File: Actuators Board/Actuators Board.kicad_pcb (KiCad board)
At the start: 2 copper layers, 50 x 50 mm, 101 parts, among them IC1 BD62120AEFJ-E2, J10 Conn_01x02_Male, J3 USB_C_Receptacle_USB2.0, J4 Conn_01x03_Male, J5 Conn_01x06_Male, J9 Conn_01x02_Male, Q1 MMDT2222A, Q2 SI2366DS, U1 ESP32-PICO-D4, U2 TPS54233D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

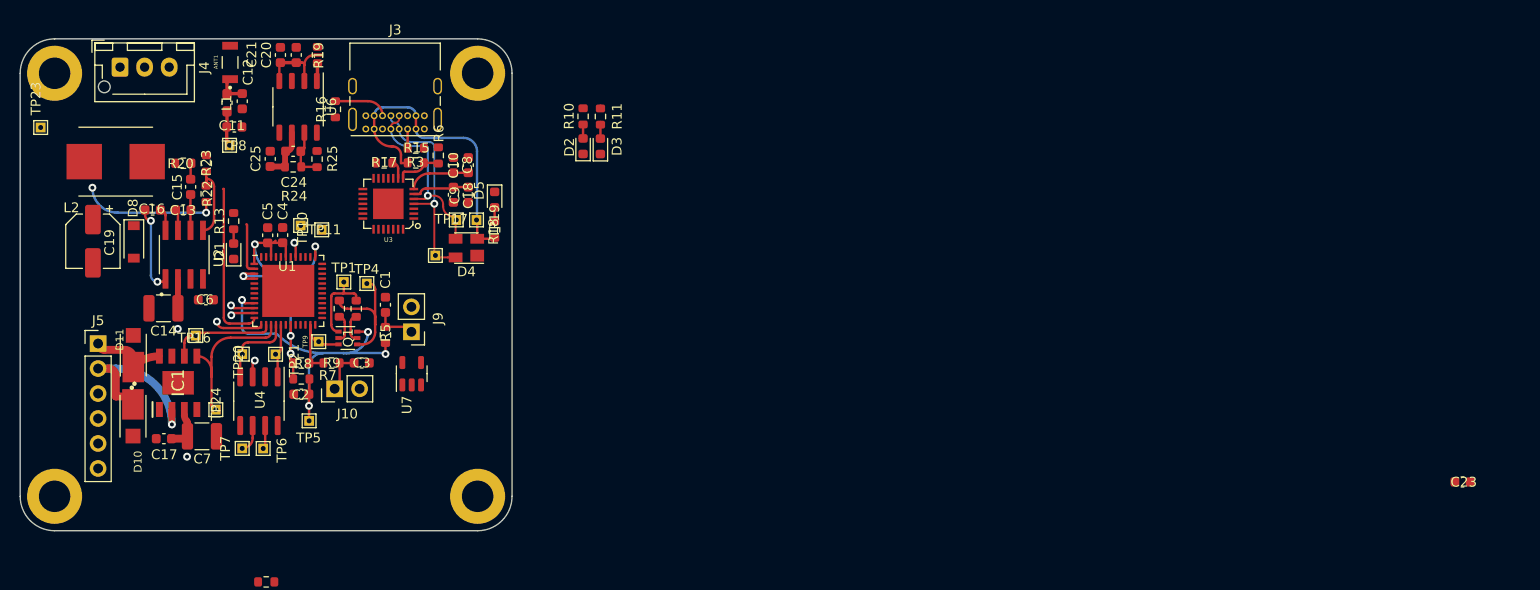
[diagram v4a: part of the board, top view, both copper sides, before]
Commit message: Added (unfilled) ground zones + antenna keepout
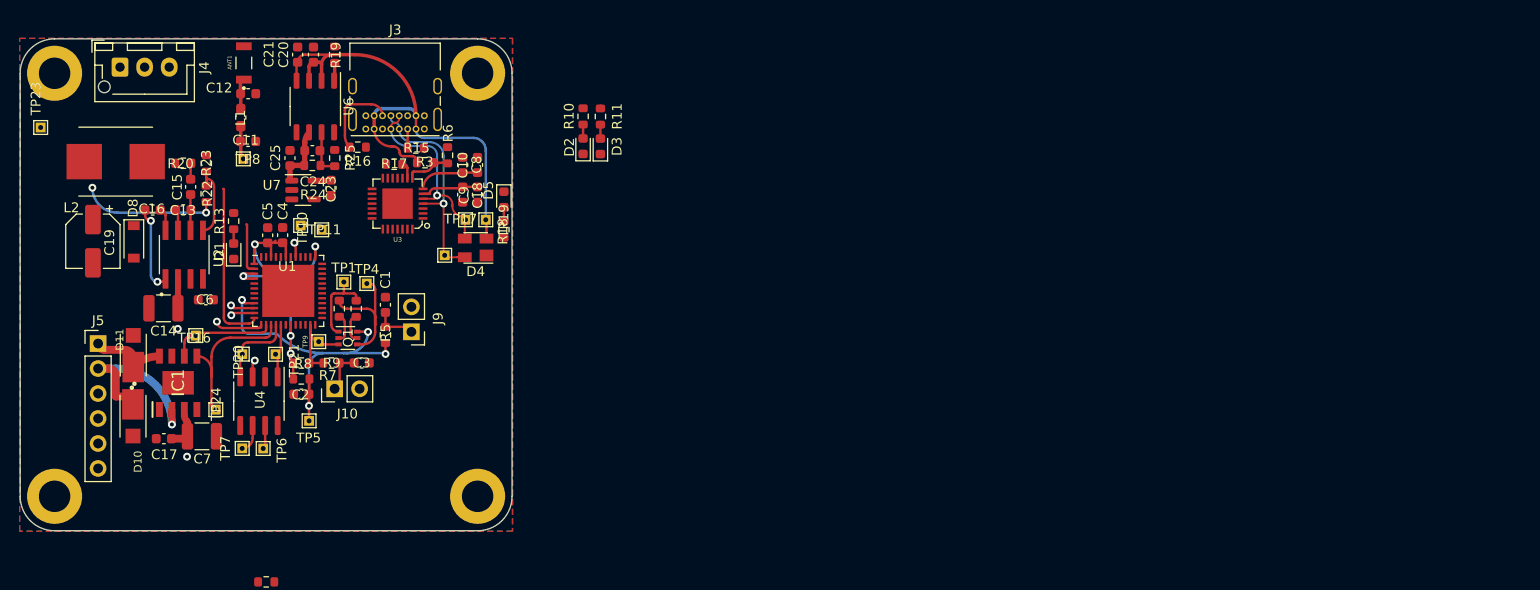
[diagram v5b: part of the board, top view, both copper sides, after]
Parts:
- moved C23 118.8 mm to (86.6, 45.1), turned to -90 degrees
- moved U7 21.7 mm to (83.8, 45.4), turned to 0 degrees
- moved R16 4.47 mm to (89.3, 41.0), turned to 180 degrees
- moved L1 2.05 mm to (77.4, 38.0)
- moved C11 2.03 mm to (78.2, 40.4)
- moved C25 2.01 mm to (82.4, 42.1)
- moved TP8 1.97 mm to (77.7, 42.2)
- moved R24 1.96 mm to (84.7, 42.9)
- moved C24 1.95 mm to (84.7, 41.4)
- moved R25 1.80 mm to (87.0, 42.1)
- moved C20 1.75 mm to (84.8, 31.6)
- moved C21 1.75 mm to (83.2, 31.6)
- moved R19 1.75 mm to (87.0, 31.6)
- moved U6 1.75 mm to (85.0, 36.9)
- moved ANT1 1.40 mm to (77.7, 32.4)
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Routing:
- net VBUS: track 40.1 -> 55.4 mm
- net Net-(J3-PadB5): track 5.58 -> 8.62 mm
- net +3V3: track 52.5 -> 54.2 mm
- net Net-(C24-Pad2): track 5.39 -> 6.52 mm
- net /USB -> UART/Data-: track 19.0 -> 19.5 mm
- added copper zone on B.Cu, net GND
- added copper zone on F.Cu, net GND

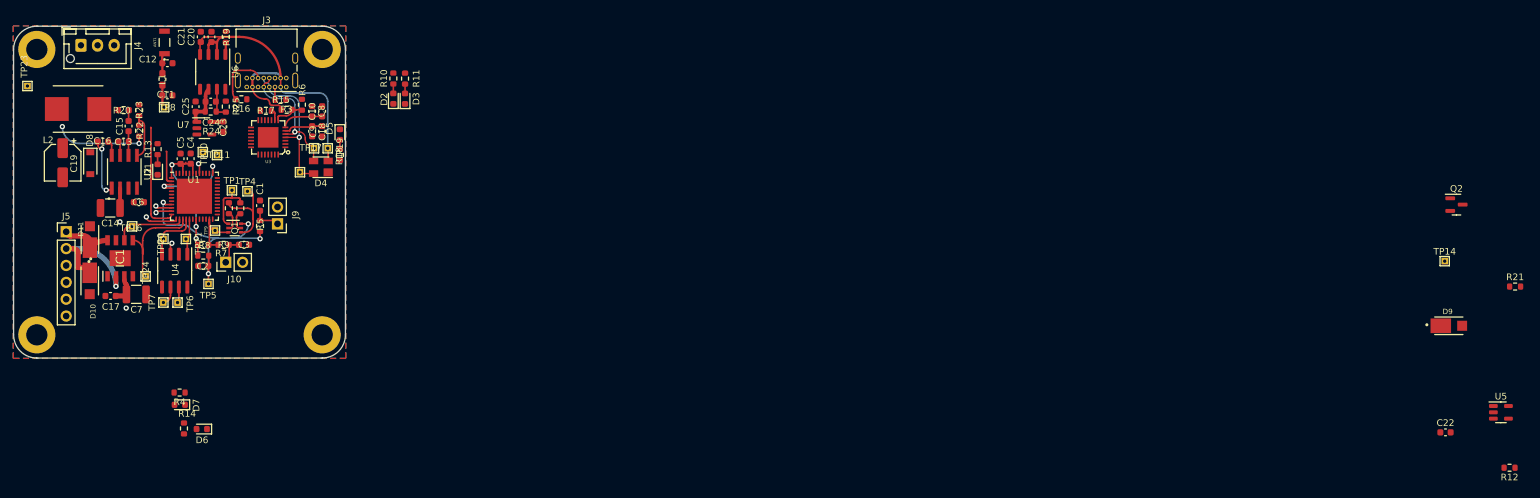
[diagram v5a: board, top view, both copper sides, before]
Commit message: Completed board layout
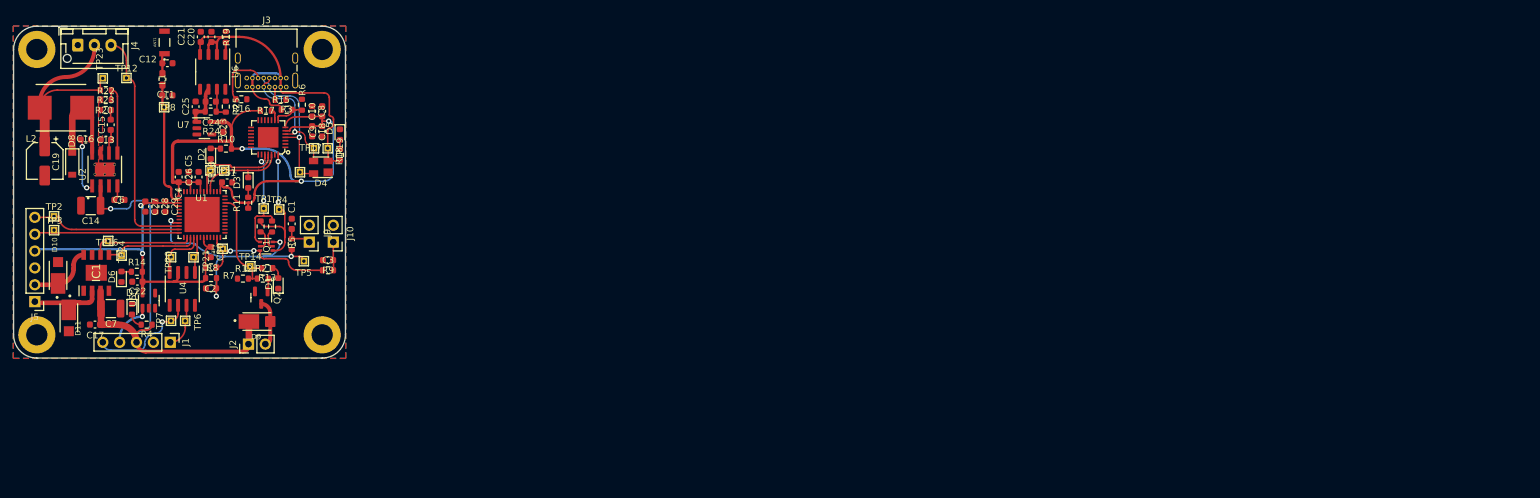
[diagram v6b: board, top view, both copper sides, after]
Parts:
- added ?: , , F.Cu at (93.7, 74.5)
- added C26: 100pF, Capacitor_SMD:C_0603_1608Metric, F.Cu at (82.9, 52.7)
- added C27: 10uF, Capacitor_SMD:C_0603_1608Metric, F.Cu at (74.8, 57.2)
- added C28: 1uF, Capacitor_SMD:C_0603_1608Metric, F.Cu at (76.4, 57.2)
- added C29: 0.1uF, Capacitor_SMD:C_0603_1608Metric, F.Cu at (77.9, 57.2)
- added C30: 0.1uF, Capacitor_SMD:C_0603_1608Metric, F.Cu at (84.7, 64.0)
- added C31: 0.1uF, Capacitor_SMD:C_0603_1608Metric, F.Cu at (87.2, 53.5)
- added J1: Conn_01x05_Male, Connector_PinHeader_2.54mm:PinHeader_1x05_P2.54mm_Vertical, F.Cu at (78.6, 77.6)
- added J2: Solenoid(Sol), Connector_PinHeader_2.54mm:PinHeader_1x02_P2.54mm_Vertical, F.Cu at (90.4, 77.9)
- added TP12: TestPoint, TestPoint:TestPoint_THTPad_1.0x1.0mm_Drill0.5mm, F.Cu at (72.0, 37.8)
- added TP2: TestPoint, TestPoint:TestPoint_THTPad_1.0x1.0mm_Drill0.5mm, F.Cu at (61.1, 58.6)
- added TP3: TestPoint, TestPoint:TestPoint_THTPad_1.0x1.0mm_Drill0.5mm, F.Cu at (61.1, 60.7)
- C4: value 10uF -> 0.1uF
- C5: value 0.1uF -> 1uF
- U2: footprint iclr:SOIC127P599X175-8N -> iclr:SOIC127P600X170-9N
- moved U5 204.4 mm to (75.4, 71.3), turned to 90 degrees
- moved C22 198.4 mm to (73.7, 68.5), turned to 180 degrees
- moved R12 193.0 mm to (89.6, 68.0)
- moved R21 188.7 mm to (92.6, 68.0), turned to 180 degrees
- moved Q2 180.6 mm to (92.3, 70.9), turned to -90 degrees
- moved TP14 180.0 mm to (90.7, 66.2)
- moved D9 179.6 mm to (91.7, 74.5)
- moved R11 30.1 mm to (90.3, 56.6), turned to 90 degrees
- moved D2 28.7 mm to (84.7, 49.2)
- moved R10 27.3 mm to (87.0, 48.5), turned to 180 degrees
- moved D3 26.8 mm to (90.3, 53.6), turned to -90 degrees
- moved D6 25.9 mm to (71.2, 67.8), turned to 90 degrees
- moved D1 25.0 mm to (94.9, 68.8)
- moved R14 24.7 mm to (73.6, 67.0), turned to 0 degrees
- moved R13 24.4 mm to (93.2, 66.5), turned to 180 degrees
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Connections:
- C4 pad 1: GND -> +3V3
- C4 pad 2: +3V3 -> GND
- IC1 pad 2: /Motor- -> /Motor+
- IC1 pad 8: /Motor+ -> /Motor-
- U1 pad 10: /Hall1 -> /ServoPWM
- U1 pad 12: /SolEN -> /Hall1
- U1 pad 13: /ServoPWM -> unconnected-(U1-Pad13)
- U1 pad 34: unconnected-(U1-Pad34) -> /SolEN
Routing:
- net +3V3: track 54.2 -> 153.6 mm, vias 6 -> 5
- net +24V: track 8.02 -> 73.4 mm, vias 2 -> 1
- net /ServoPWM: track 5.02 -> 35.4 mm, vias 1 -> 0
- net /Hall2: track 2.46 -> 22.9 mm, vias 1 -> 0
- net /Hall1: track 2.51 -> 22.4 mm, vias 1 -> 0
- net +6V: track 14.2 -> 32.5 mm, vias 2 -> 0
- net /RXD: track 1.56 -> 15.8 mm, vias 1 -> 0
- net /TXD: track 0.00 -> 14.0 mm
- net /CAN_LOW: track 2.89 -> 16.5 mm, vias 0 -> 1
- net /BOOT: track 9.52 -> 22.7 mm, vias 0 -> 2
- net Net-(C16-Pad2): track 2.34 -> 15.0 mm
- net /LNA_IN: track 8.61 -> 19.0 mm
- net /Motor-: track 19.5 -> 10.6 mm, vias 1 -> 0
- net /DTR: track 13.3 -> 22.2 mm, vias 0 -> 2
- net /RTS: track 8.47 -> 17.0 mm, vias 0 -> 2
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
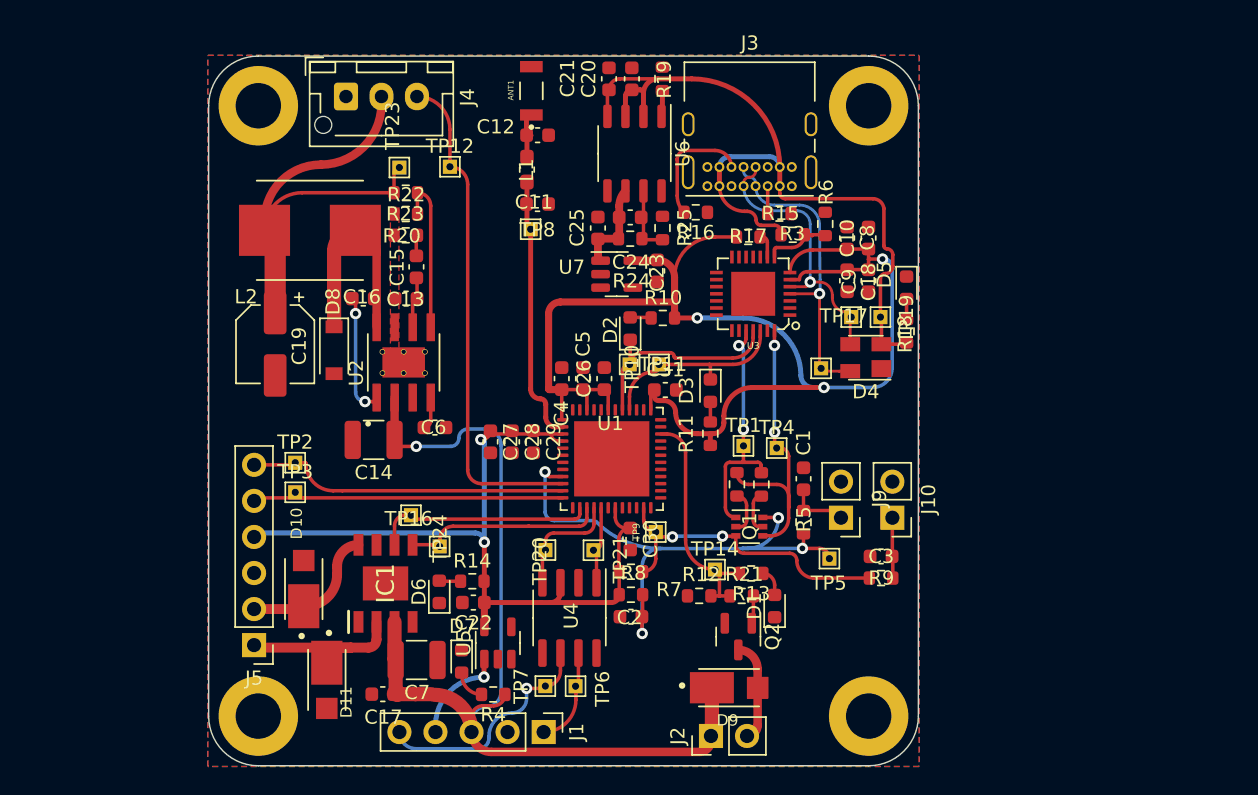
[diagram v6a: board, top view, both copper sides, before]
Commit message: Moved esp closer to the antenna
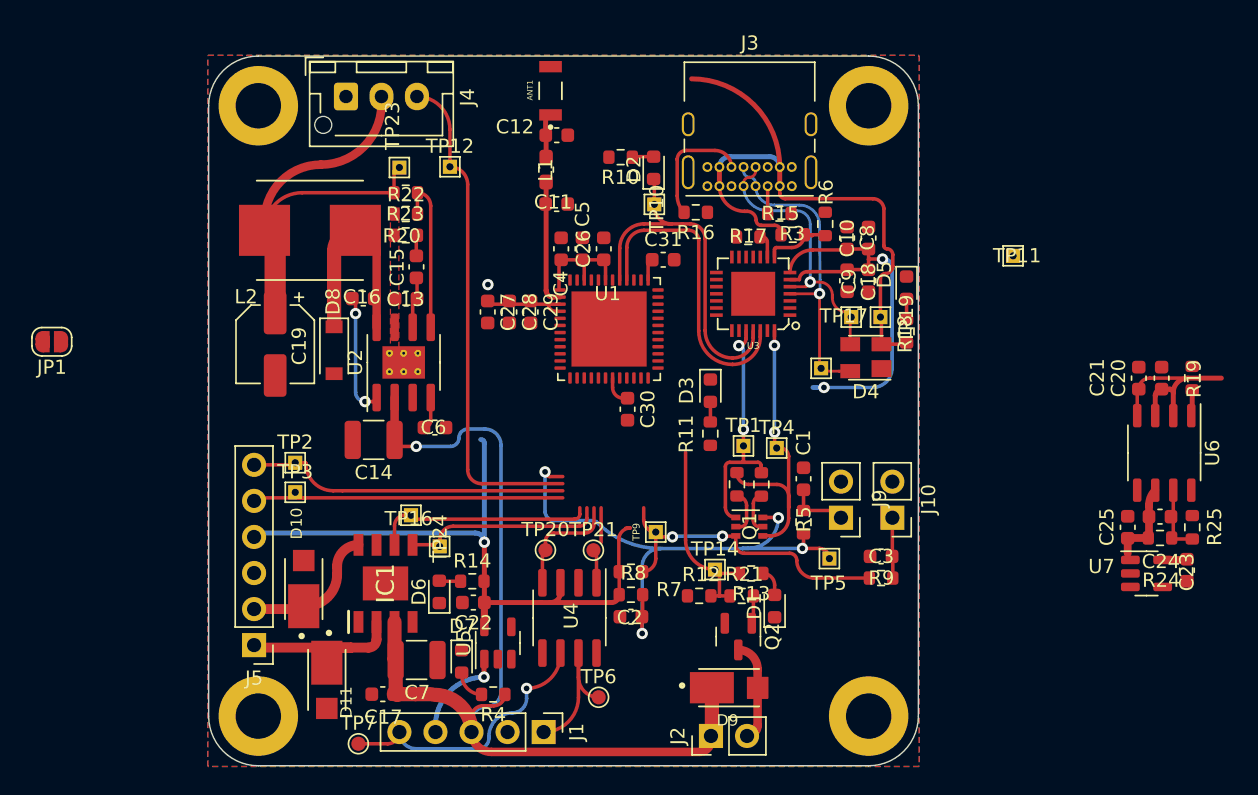
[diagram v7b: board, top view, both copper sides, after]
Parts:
- removed TP8: TestPoint, TestPoint:TestPoint_THTPad_1.0x1.0mm_Drill0.5mm
- added JP1: SolderJumper_2_Open, Jumper:SolderJumper-2_P1.3mm_Open_RoundedPad1.0x1.5mm, F.Cu at (44.0, 50.1)
- TP20, TP21, TP6, TP7: footprint TestPoint:TestPoint_THTPad_1.0x1.0mm_Drill0.5mm -> TestPoint:TestPoint_Pad_D1.0mm
- U2: footprint iclr:SOIC127P600X170-9N -> Package_SO:SOIC-8-1EP_3.9x4.9mm_P1.27mm_EP2.29x3mm_ThermalVias
- moved C20 42.9 mm to (122.1, 52.7)
- moved C21 42.9 mm to (120.5, 52.7)
- moved C23 42.9 mm to (123.9, 66.2)
- moved C24 42.9 mm to (122.0, 62.5)
- moved C25 42.9 mm to (119.8, 63.2)
- moved R19 42.9 mm to (124.3, 52.7)
- moved R24 42.9 mm to (122.0, 64.0)
- moved R25 42.9 mm to (124.3, 63.2)
- moved U6 42.9 mm to (122.3, 58.0)
- moved U7 42.9 mm to (121.1, 66.5)
- moved TP11 26.1 mm to (111.7, 44.1)
- moved TP7 13.8 mm to (65.5, 78.5)
- moved R10 11.7 mm to (84.0, 37.1), turned to 0 degrees
- moved D2 11.4 mm to (86.3, 37.9)
- moved TP10 11.4 mm to (86.4, 40.5)
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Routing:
- net +3V3: track 153.6 -> 95.6 mm, vias 5 -> 4
- net /LNA_IN: track 19.0 -> 8.87 mm
- net /RXD: track 15.8 -> 25.7 mm
- net /TXD: track 14.0 -> 21.8 mm
- net /CAN_HIGH: track 6.89 -> 10.7 mm
- net /CAN_LOW: track 16.5 -> 19.3 mm
- net /SolEN: track 17.6 -> 15.1 mm
- net /CAN_TX: track 5.69 -> 4.86 mm
- net Net-(C24-Pad2): track 6.52 -> 5.95 mm

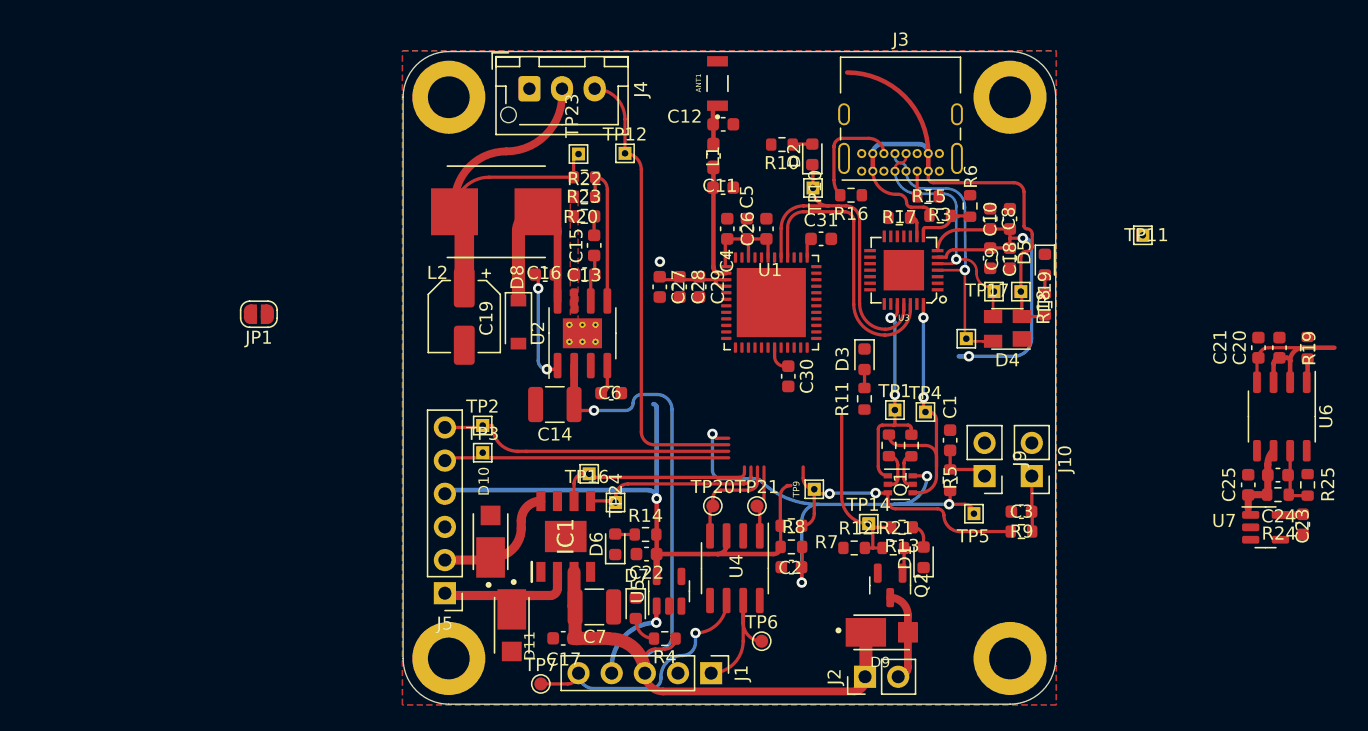
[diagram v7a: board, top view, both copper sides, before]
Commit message: redone layout to match new esp position
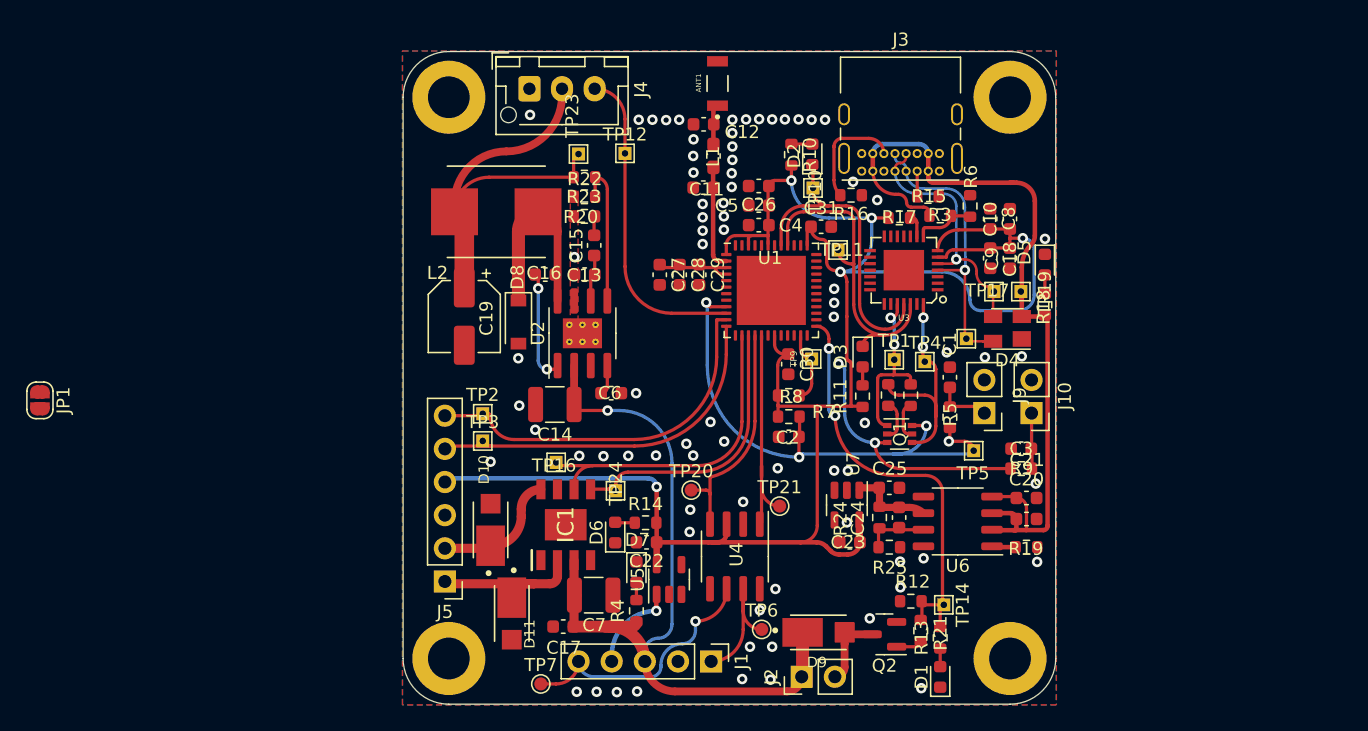
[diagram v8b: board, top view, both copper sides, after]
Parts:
- moved C23 34.7 mm to (89.2, 67.6), turned to 180 degrees
- moved R25 32.4 mm to (92.2, 68.0), turned to 0 degrees
- moved U7 32.1 mm to (89.0, 64.8), turned to -90 degrees
- moved R24 30.6 mm to (91.5, 65.7), turned to -90 degrees
- moved C24 29.2 mm to (93.0, 65.7), turned to 90 degrees
- moved C25 27.5 mm to (92.2, 63.4), turned to 180 degrees
- moved R19 26.4 mm to (102.8, 68.0), turned to 0 degrees
- moved U6 26.1 mm to (97.5, 66.0), turned to 180 degrees
- moved C20 23.4 mm to (102.8, 65.8), turned to 180 degrees
- moved TP11 23.4 mm to (88.3, 45.2)
- moved C21 21.2 mm to (102.8, 64.2), turned to 180 degrees
- moved JP1 18.0 mm to (27.2, 56.7), turned to -90 degrees
- moved R7 9.98 mm to (84.5, 58.0)
- moved C2 9.98 mm to (84.5, 59.5)
- moved R8 9.98 mm to (84.5, 56.4)
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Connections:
- U1 pad 25: unconnected-(U1-Pad25) -> /SolEN
- U1 pad 34: /SolEN -> unconnected-(U1-Pad34)
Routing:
- net +3V3: track 95.6 -> 154.6 mm, vias 4 -> 5
- net /SolEN: track 15.1 -> 32.7 mm, vias 0 -> 2
- net /CAN_TX: track 4.86 -> 18.4 mm
- net /ServoPWM: track 35.4 -> 24.5 mm
- net +24V: track 73.4 -> 63.6 mm
- net /HBridgeDIR2: track 15.6 -> 25.3 mm
- net /CAN_RX: track 8.24 -> 17.6 mm
- net /HBridgeDIR1: track 15.3 -> 22.7 mm
- net /Hall2: track 22.9 -> 28.9 mm
- net /Hall1: track 22.4 -> 28.1 mm
- net VBUS: track 58.7 -> 64.3 mm
- net /DTR: track 22.2 -> 18.1 mm
- net /RTS: track 17.0 -> 13.2 mm
- net /BOOT: track 22.7 -> 25.9 mm
- net /TXD: track 21.8 -> 24.8 mm
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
